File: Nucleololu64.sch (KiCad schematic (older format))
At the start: 74 parts, among them CN1 CONN_02X19, CN2 CONN_02X19, J1 CONN_02X02, J2 CONN_02X02, J3 CONN_01X03, P1 PT_2,5-2-5,0-H, P10 KK-2.54-4W, P11 PT_2,5-2-5,0-H, P12 PT_2,5-2-5,0-H, P13 KK-2.54-4W, P14 KK-2.54-4W, P15 PT_1,5-2-3,5-H, P2 KK-2.54-4W, P3 KK-2.54-4W, P4 HEADER_6, P5 HEADER_6X2, P6 CONN_02X02, P7 KK-2.54-4W, P8 KK-2.54-4W, P9 KK-2.54-4W, Q1 IRLB8743PBF, Q2 IRLB8743PBF, Q3 IRLB8743PBF, U1 TPS5420, U2 Pololu, U3 Pololu, U5 Pololu, U6 Pololu

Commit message: batch commit rev.1
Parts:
- removed P4: HEADER_6, Pin_Headers:Pin_Header_Straight_1x06_Pitch2.54mm, symbol HEADER_6
- removed P5: HEADER_6X2, Pin_Headers:Pin_Header_Straight_2x06_Pitch2.54mm, symbol HEADER_6x2
- added D3, D5, D7: LED, LEDs:LED_0603, symbol LED
- added F1: Fuse, Fuse_Holders_and_Fuses:Fuse_SMD1206_HandSoldering, symbol Fuse
- added J2: CONN_01X06, Pin_Headers:Pin_Header_Straight_1x06_Pitch2.54mm, symbol CONN_01X06
- added J3: CONN_02X06, Pin_Headers:Pin_Header_Straight_2x06_Pitch2.54mm, symbol CONN_02X06
- added R13, R16, R23: 10k, Resistors_SMD:R_0805_HandSoldering, symbol R
- P11: renamed from P13; footprint Extra:CONN_KK_2.54_4W -> Connectors_Molex:Molex_KK-6410-04_04x2.54mm_Straight
- P12: renamed from P14; footprint Extra:CONN_KK_2.54_4W -> Connectors_Molex:Molex_KK-6410-04_04x2.54mm_Straight
- P2, P3: footprint Extra:CONN_KK_2.54_4W -> Pin_Headers:Pin_Header_Straight_1x04_Pitch2.54mm
- P5: renamed from P7; footprint Extra:CONN_KK_2.54_4W -> Connectors_Molex:Molex_KK-6410-04_04x2.54mm_Straight
- P6: renamed from P8; footprint Extra:CONN_KK_2.54_4W -> Connectors_Molex:Molex_KK-6410-04_04x2.54mm_Straight
- P7: renamed from P9; footprint Extra:CONN_KK_2.54_4W -> Pin_Headers:Pin_Header_Straight_1x04_Pitch2.54mm
- P8: renamed from P10; footprint Extra:CONN_KK_2.54_4W -> Pin_Headers:Pin_Header_Straight_1x04_Pitch2.54mm
- Q1, Q2, Q3: footprint Extra:TO-220AB -> TO_SOT_Packages_THT:TO-220-3_Vertical
- renumbered D5 to D2, D2 to D4, D3 to D6, D4 to D8, F1 to F2, F2 to F3, J3 to J4, J2 to J5, P12 to P10, P15 to P13, P6 to P4, P11 to P9, R3 to R1, R13 to R14, R14 to R15, R15 to R17, R16 to R18, R17 to R19, R4 to R2, R18 to R20, R20 to R21, R21 to R22, R19 to R24, R22 to R25, R23 to R26, R24 to R27, R1 to R3, R7 to R4, R8 to R5, R2 to R6, R5 to R7, R6 to R8, U5 to U4, U6 to U5
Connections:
- wire segments 237 -> 263
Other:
- note added: "J3 placed such that it\nplugs into the Nucleo 64 \nboard J5 jumper."
- note added: "R2 = (R1 * 1.221) / (VOUT - 1.221)\n\nmod to get 5v5"
- note added: "double check with assignments on nucleo\n"
- note removed: "50V"
- note removed: "J3 placed such that it plugs\ninto the Nucleo 64 board J5 \njumper."
- note removed: "R2 = (R1 * 1.221) / (VOUT - 1.221)"
- note removed: "TO-220"
- moved on the sheet: C1, C2, C3, C4, C5, C6, D1, D2, D4, D6, D8, F2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

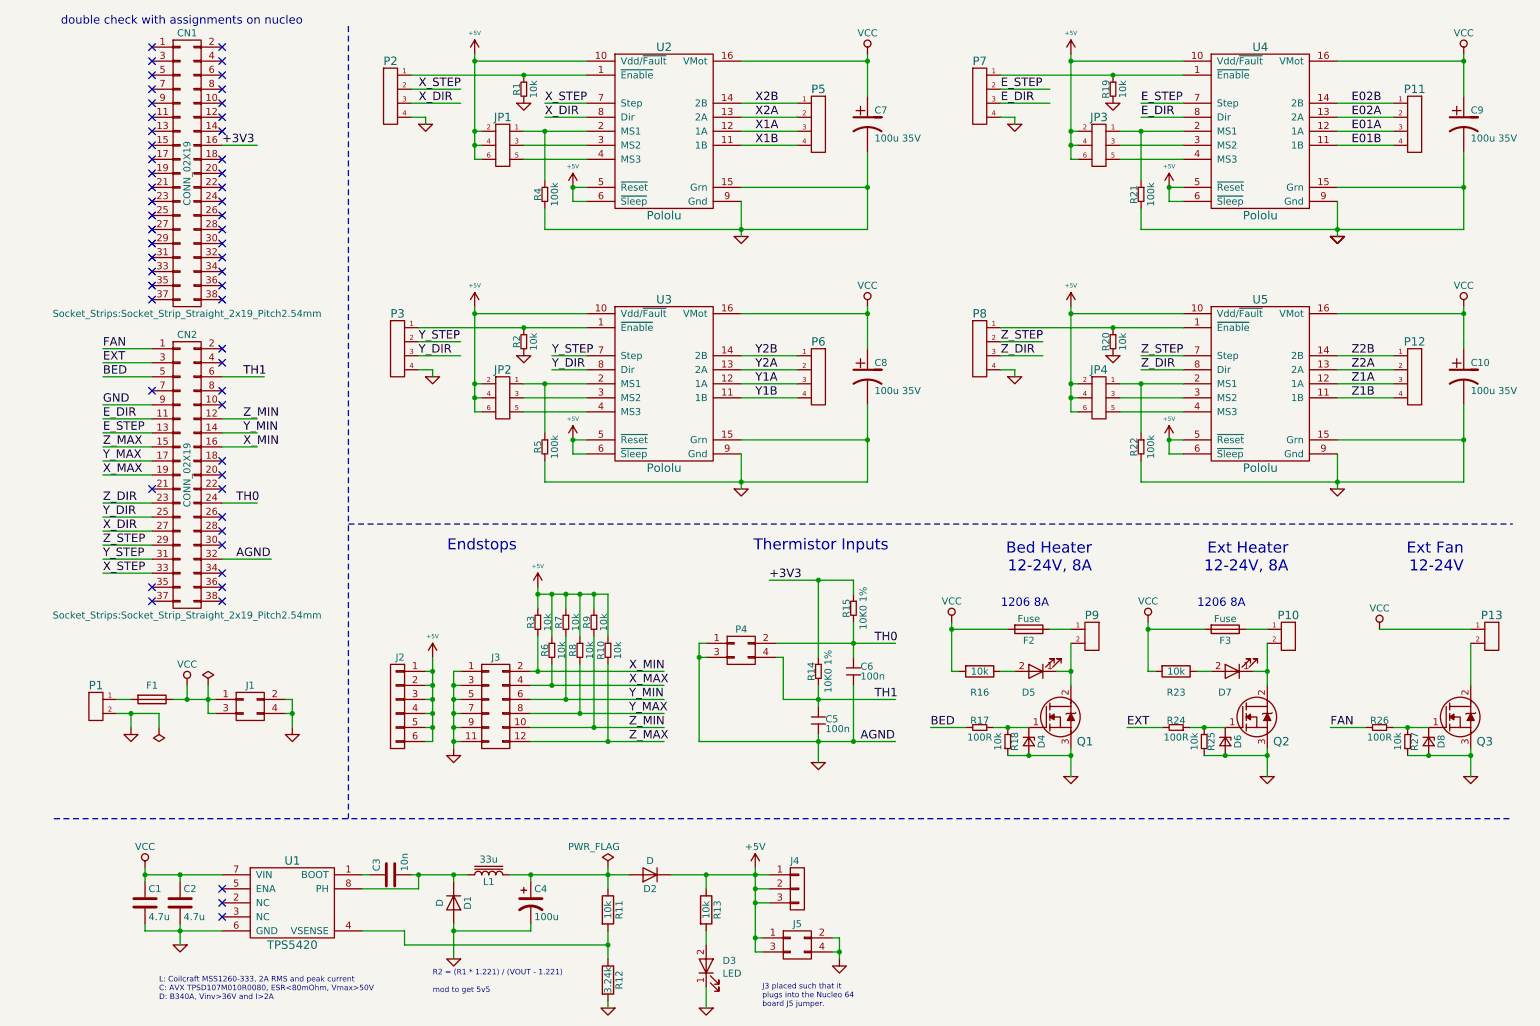
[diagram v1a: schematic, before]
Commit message: added many manf#
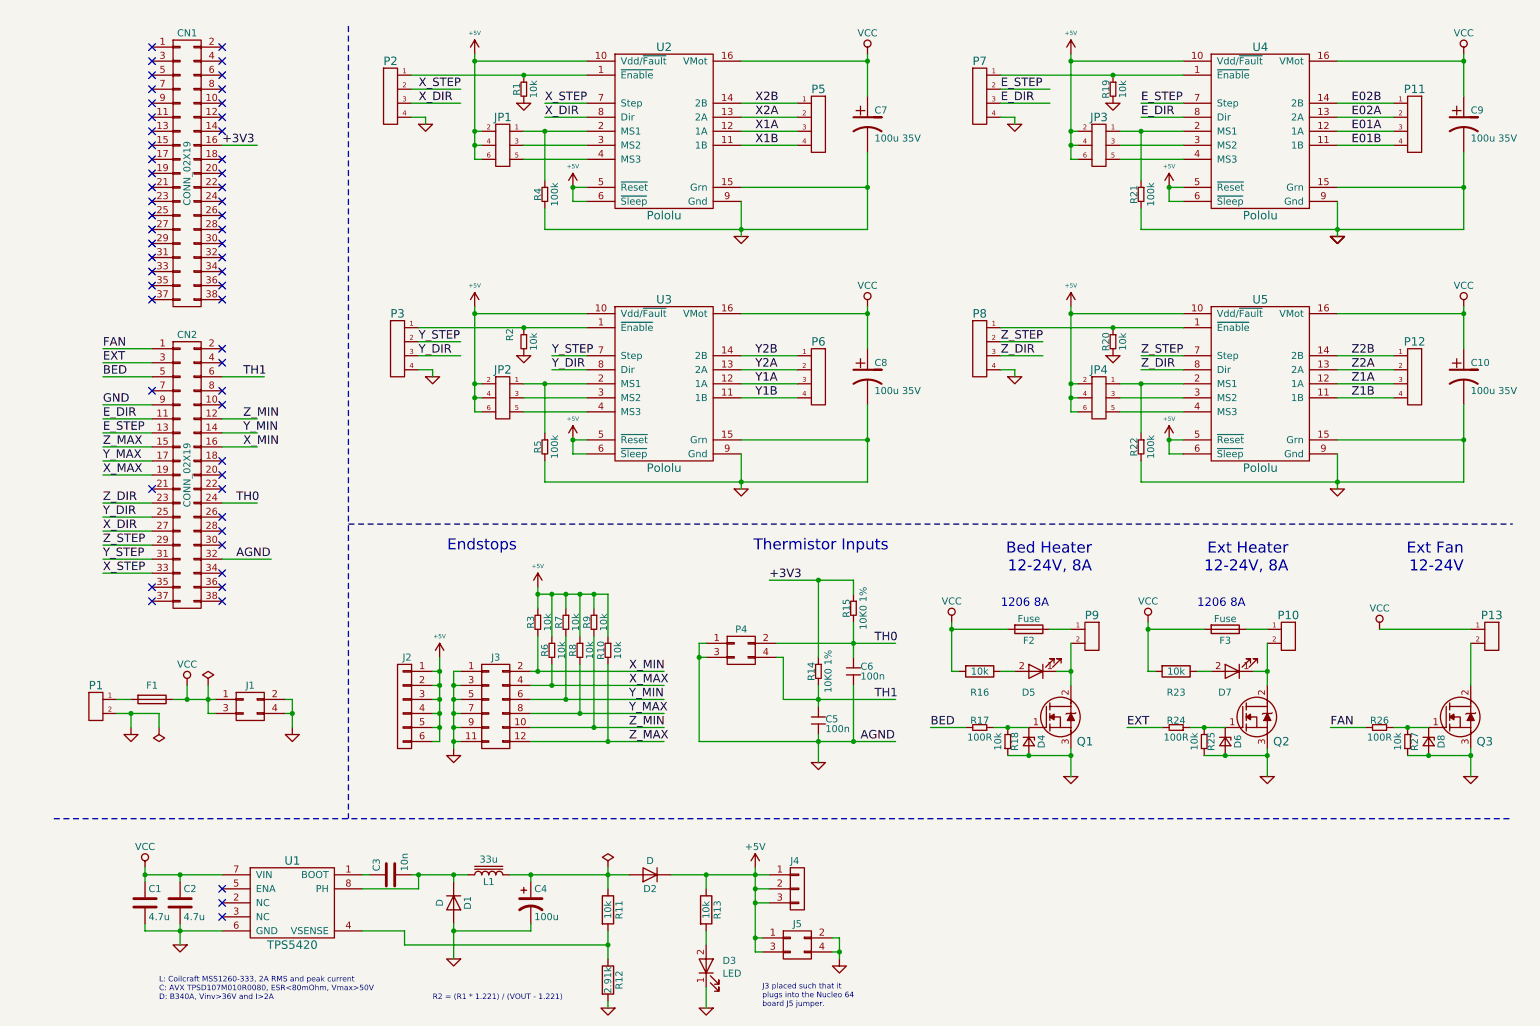
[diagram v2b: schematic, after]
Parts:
- C1: Man (none) -> Murata; manf# (none) -> GRM21BR61H475ME51L
- C10, C7, C8, C9: PartNo UCD1V101MCL6GS -> (none); manf# (none) -> UWT1H101MNL1GS
- C2: manf# (none) -> GRM21BR61H475ME51L
- C4: manf# (none) -> TPSD107M010R0080
- CN1, CN2: manf# (none) -> 929974-01-19-RK
- D1, D2: manf# (none) -> B340A-13-F
- D3, D5, D7: manf# (none) -> AP2012EC
- F1: manf# (none) -> CC12H20A-TR
- F2, F3: manf# (none) -> CC12H8A-TR
- J1, J5, P4: manf# (none) -> 961204-6804-AR
- J2: manf# (none) -> M20-9770642
- J3: manf# (none) -> M20-9760642
- J4: manf# (none) -> M20-7820346
- JP1, JP2, JP3, JP4: PartNo M20-9980345 -> (none); manf# (none) -> M20-9980345
- L1: manf# (none) -> MSS1260-333MLD
- P1: Mfg Phoenix -> (none); PartNo 1935776 -> (none); manf# (none) -> 1935776
- P11, P12, P5, P6: PartNo 22-23-2041 -> (none); manf# (none) -> 22-23-2041
- P2, P3, P7, P8: manf# (none) -> M20-9990445
- Q1, Q2, Q3: PartNo IRLB8743PBF -> (none); manf# (none) -> IRLB8743PBF
- R1, R19, R20, R21, R22, R4, R5: PartNo RMCF0603FT100K -> (none); manf# (none) -> RMCF0603FT100K
- R10, R3, R6, R7, R8: PartNo RMCF0603FT10K0 -> (none); manf# (none) -> RMCF0603FT10K0
- R11: manf# (none) -> RC0805FR-0710KL
- R12: value 3.24k -> 2.91k
- R14, R15: PartNo RMCF0603FT2K00 -> (none); manf# (none) -> RC0805FR-0710KL
- U1: manf# (none) -> TPS5420DR
- U2: PartNo DRV8825 -> (none); manf# (none) -> M20-7820842
- U3, U4, U5: manf# (none) -> M20-7820842
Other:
- note added: "R2 = (R1 * 1.221) / (VOUT - 1.221)"
- note removed: "R2 = (R1 * 1.221) / (VOUT - 1.221)\n\nmod to get 5v5"
- note removed: "double check with assignments on nucleo\n"
- moved on the sheet: J2
